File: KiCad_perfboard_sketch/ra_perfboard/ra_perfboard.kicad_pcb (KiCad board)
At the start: 2 copper layers, 141 x 71.1 mm, 20 parts, among them J1 M1, J10 L6, J2 M2, J3 Terminal, J4 USART, J5 L3, J6 L1, J7 L2, J8 L4, J9 L5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

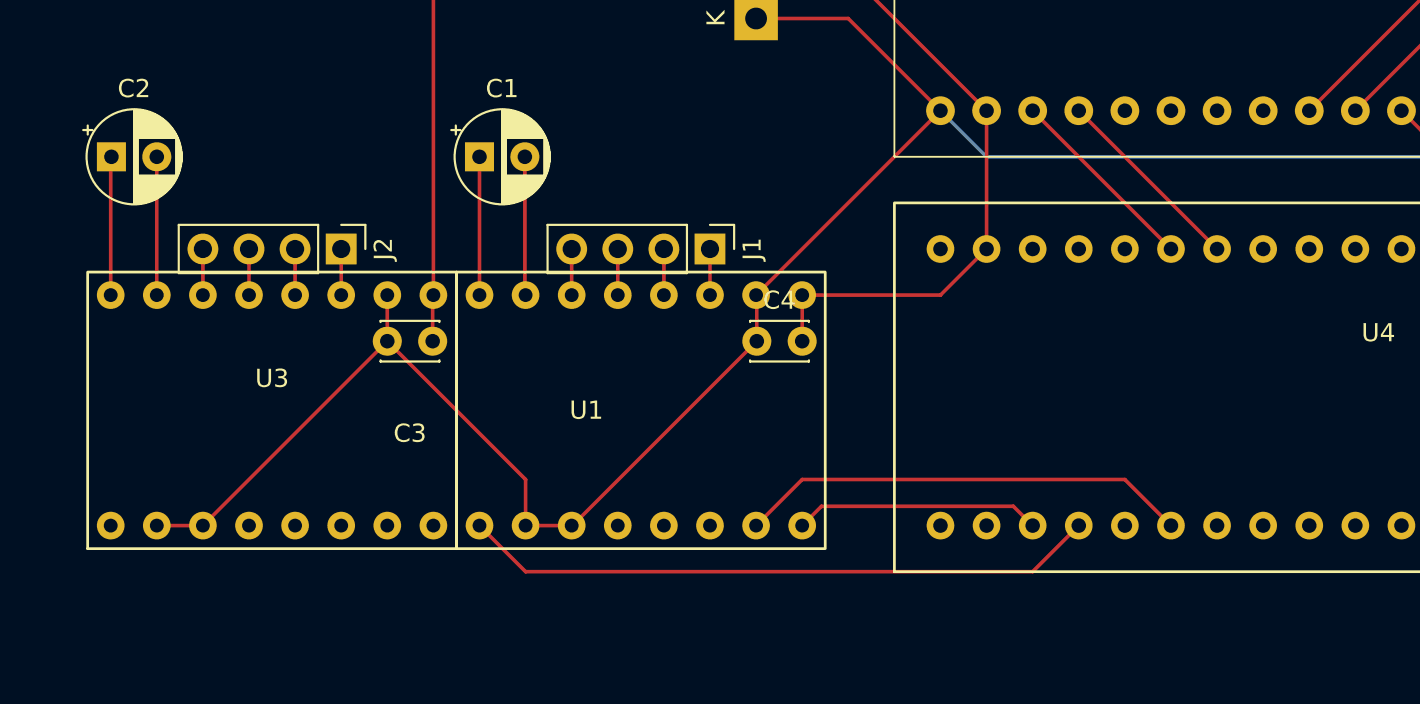
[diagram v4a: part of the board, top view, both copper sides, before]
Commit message: Removed bug in LUT set speed function. Updates to MATLAB GUI and KiCad perfboard. Successfully tested TCA9548A library.
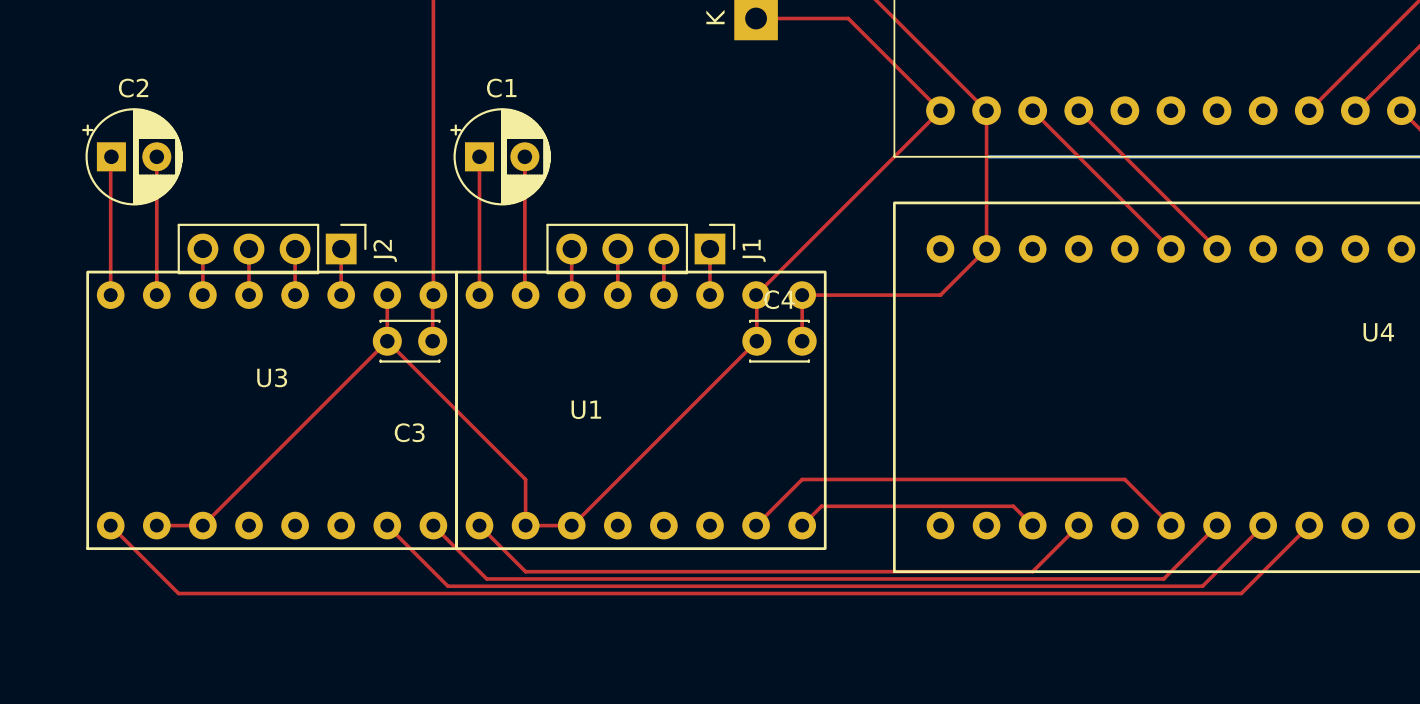
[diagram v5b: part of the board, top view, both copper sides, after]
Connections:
- U4 pad 10: /M2_EN -> unconnected-(U4-PA4-Pad10)
- U4 pad 11: /M2_STEP -> unconnected-(U4-PA5-Pad11)
- U4 pad 7: unconnected-(U4-PA1-Pad7) -> /M2_DIR
- U4 pad 8: unconnected-(U4-PA2-Pad8) -> /M2_STEP
- U4 pad 9: /M2_DIR -> /M2_EN
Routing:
- net /M2_EN: track 0.00 -> 69.1 mm
- net /M2_STEP: track 0.00 -> 51.0 mm
- net /M2_DIR: track 0.00 -> 45.6 mm
- net +3V3: track 146.0 -> 142.4 mm
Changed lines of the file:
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@@
 	(net 28 "unconnected-(U4-PA8-Pad36)")
 	(net 29 "unconnected-(U4-PB3-Pad30)")
-	(net 30 "unconnected-(U4-PA1-Pad7)")
+	(net 30 "unconnected-(U4-PA4-Pad10)")
 	(net 31 "/USART1_RX")
 	(net 32 "unconnected-(U4-PB1-Pad15)")
@@
 	(net 73 "/SDA5")
 	(net 74 "/SCL5")
-	(net 75 "unconnected-(U4-PA2-Pad8)")
+	(net 75 "unconnected-(U4-PA5-Pad11)")
 	(net 76 "unconnected-(U4-PA15-Pad31)")
 	(footprint "TerminalBlock_Phoenix:TerminalBlock_Phoenix_MKDS-1,5-2-5.08_1x02_P5.08mm_Horizontal"
@@
 			(layers "*.Cu" "*.Mask" "B.Adhes")
 			(remove_unused_layers no)
-			(net 30 "unconnected-(U4-PA1-Pad7)")
+			(net 22 "/M2_DIR")
 			(pinfunction "PA1")
 			(pintype "bidirectional")
@@
 			(layers "*.Cu" "*.Mask" "B.Adhes")
 			(remove_unused_layers no)
-			(net 75 "unconnected-(U4-PA2-Pad8)")
+			(net 21 "/M2_STEP")
 			(pinfunction "PA2")
 			(pintype "bidirectional")
@@
 			(layers "*.Cu" "*.Mask" "B.Adhes")
 			(remove_unused_layers no)
-			(net 22 "/M2_DIR")
+			(net 20 "/M2_EN")
 			(pinfunction "PA3")
 			(pintype "bidirectional")
@@
 			(layers "*.Cu" "*.Mask" "B.Adhes")
 			(remove_unused_layers no)
-			(net 20 "/M2_EN")
+			(net 30 "unconnected-(U4-PA4-Pad10)")
 			(pinfunction "PA4")
 			(pintype "bidirectional")
@@
 			(layers "*.Cu" "*.Mask" "B.Adhes")
 			(remove_unused_layers no)
-			(net 21 "/M2_STEP")
+			(net 75 "unconnected-(U4-PA5-Pad11)")
 			(pinfunction "PA5")
 			(pintype "bidirectional")
@@
 	)
 	(segment
-		(start 149.86 88.9)
-		(end 147.32 86.36)
-		(width 0.2)
-		(layer "B.Cu")
-		(net 7)
-	)
-	(segment
 		(start 187.96 88.9)
 		(end 149.86 88.9)
@@
 	)
 	(segment
+		(start 105.343 112.963)
+		(end 163.897 112.963)
+		(width 0.2)
+		(layer "F.Cu")
+		(net 20)
+	)
+	(segment
+		(start 163.897 112.963)
+		(end 167.64 109.22)
+		(width 0.2)
+		(layer "F.Cu")
+		(net 20)
+	)
+	(segment
+		(start 101.6 109.22)
+		(end 105.343 112.963)
+		(width 0.2)
+		(layer "F.Cu")
+		(net 20)
+	)
+	(segment
+		(start 116.84 109.22)
+		(end 120.182 112.562)
+		(width 0.2)
+		(layer "F.Cu")
+		(net 21)
+	)
+	(segment
+		(start 120.182 112.562)
+		(end 161.758 112.562)
+		(width 0.2)
+		(layer "F.Cu")
+		(net 21)
+	)
+	(segment
+		(start 161.758 112.562)
+		(end 165.1 109.22)
+		(width 0.2)
+		(layer "F.Cu")
+		(net 21)
+	)
+	(segment
+		(start 122.321 112.161)
+		(end 119.38 109.22)
+		(width 0.2)
+		(layer "F.Cu")
+		(net 22)
+	)
+	(segment
+		(start 159.619 112.161)
+		(end 122.321 112.161)
+		(width 0.2)
+		(layer "F.Cu")
+		(net 22)
+	)
+	(segment
+		(start 162.56 109.22)
+		(end 159.619 112.161)
+		(width 0.2)
+		(layer "F.Cu")
+		(net 22)
+	)
+	(segment

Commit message: Final commit after submitting project. Currently no plans to proegress in this project any further.
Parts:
- added C5: M3_Cap, Capacitor_THT:CP_Radial_D5.0mm_P2.50mm, F.Cu at (80.1, 102.3)
- added C6: 100nF, Capacitor_THT:C_Disc_D3.0mm_W2.0mm_P2.50mm, F.Cu at (116.6, 107.8)
- added C7: M4_Cap, Capacitor_THT:CP_Radial_D5.0mm_P2.50mm, F.Cu at (100.1, 102.3)
- added C8: 100nF, Capacitor_THT:C_Disc_D3.0mm_W2.0mm_P2.50mm, F.Cu at (95.8, 107.8)
- added J11: M3, Connector_PinHeader_2.54mm:PinHeader_1x04_P2.54mm_Vertical, F.Cu at (92.6, 107.8)
- added J12: M4, Connector_PinHeader_2.54mm:PinHeader_1x04_P2.54mm_Vertical, F.Cu at (113.1, 107.8)
- added U6: ~, stm32_ra_board_footprints:TMC2208_Board_Footprint, F.Cu at (88.7, 117.1)
- added U7: ~, stm32_ra_board_footprints:TMC2208_Board_Footprint, F.Cu at (109.2, 117.1)
- moved C4 23.8 mm to (156.3, 113.3)
- moved D1 23.8 mm to (156.2, 95.6)
- moved J3 23.8 mm to (102.9, 77.8)
- moved U2 23.8 mm to (180.4, 91.8)
- moved U4 23.8 mm to (190.5, 115.9)
- moved C1 23.8 mm to (141.0, 103.2)
- moved C2 23.8 mm to (120.7, 103.2)
- moved J2 23.8 mm to (133.4, 108.3)
- moved U3 23.8 mm to (129.6, 117.2)
- moved U5 23.8 mm to (130.8, 82.9)
- moved C3 23.8 mm to (135.9, 113.3)
- moved J1 23.8 mm to (153.7, 108.3)
- moved J4 23.8 mm to (199.4, 100.6)
- moved J5 23.8 mm to (207.0, 95.6)
- moved J7 23.8 mm to (207.0, 85.4)
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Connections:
- U4 pad 10: unconnected-(U4-PA4-Pad10) -> /M3_EN
- U4 pad 11: unconnected-(U4-PA5-Pad11) -> /M3_DIR
- U4 pad 12: unconnected-(U4-PA6-Pad12) -> /M3_STEP
- U4 pad 31: unconnected-(U4-PA15-Pad31) -> /M4_DIR
- U4 pad 32: unconnected-(U4-PA12-Pad32) -> /M4_EN
- U4 pad 33: unconnected-(U4-PA11-Pad33) -> /M4_STEP
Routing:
- net GND: track 172.2 -> 194.5 mm
- net +24V: track 24.0 -> 41.2 mm
